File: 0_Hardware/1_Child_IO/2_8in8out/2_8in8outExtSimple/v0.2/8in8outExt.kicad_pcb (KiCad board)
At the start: 2 copper layers, 101.6 x 42 mm, 73 parts, among them P1 CONN_10X2, Q1 PNP, Q10 NPN, Q11 NPN, Q12 NPN, Q13 NPN, Q14 NPN, Q15 NPN, Q16 NPN, Q19 NPN, Q2 PNP, Q3 PNP, Q4 PNP, Q5 PNP, Q6 PNP, Q7 PNP, Q8 PNP, Q9 NPN, SW1 SKQGAKE010

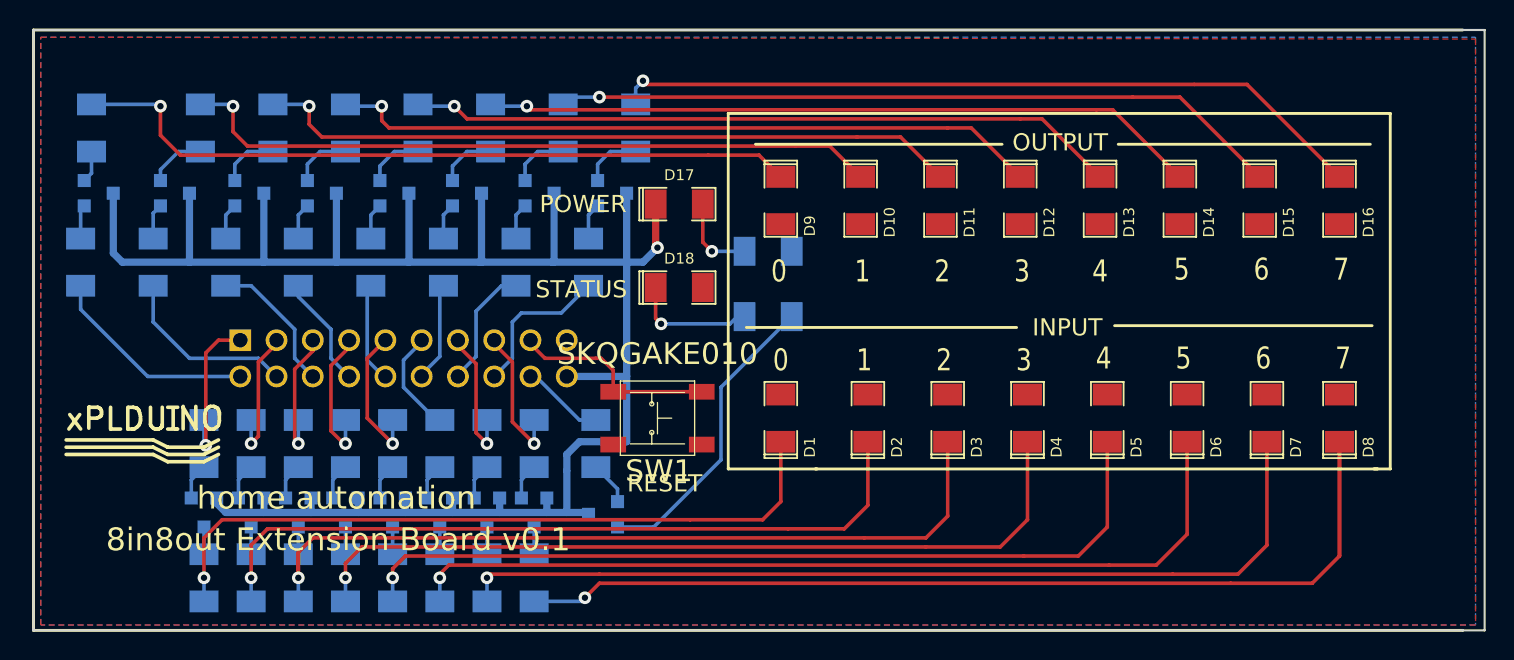
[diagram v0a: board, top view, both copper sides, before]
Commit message: IN8R8: remplacement empreinte PNP et NPN par SOT-23 standard, agencement des leds comme carte IN4DIM4
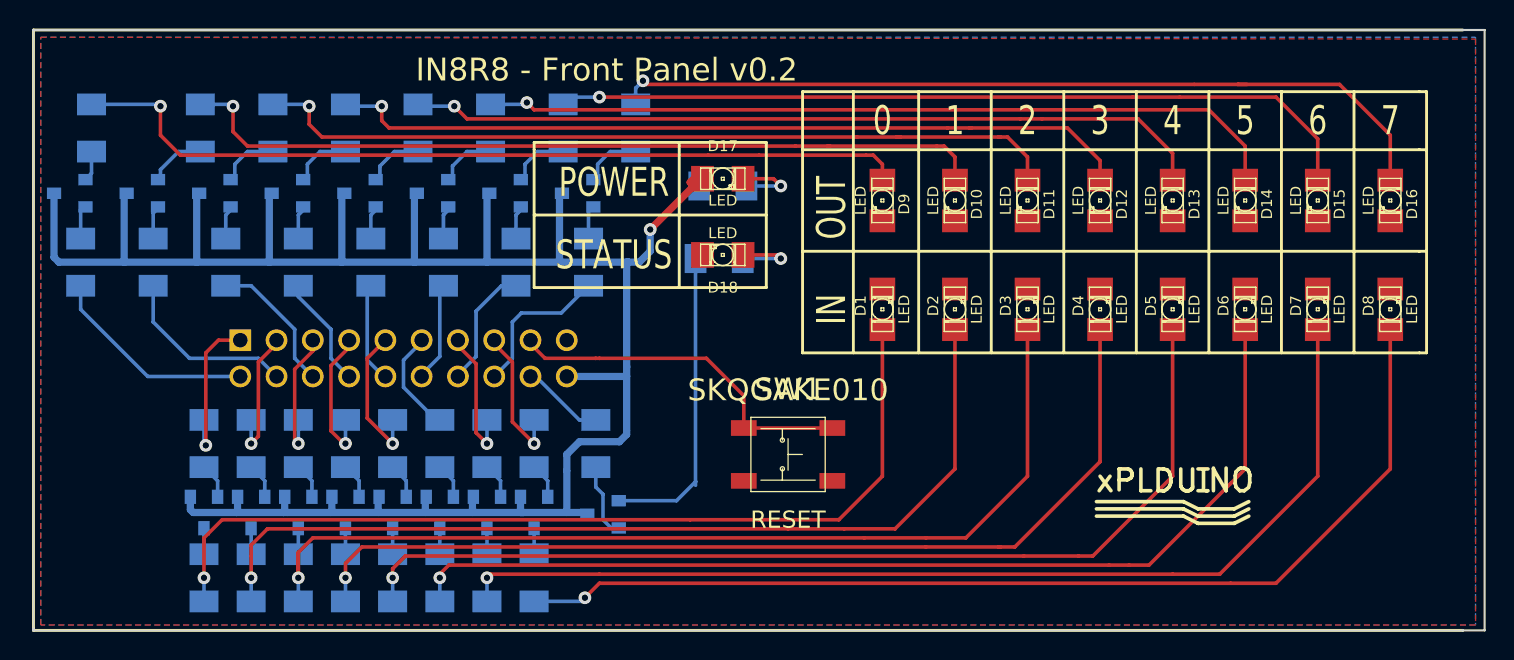
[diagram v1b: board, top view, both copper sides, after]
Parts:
- D1, D10, D11, D12, D13, D14, D15, D16, D17, D18, D2, D3, D4, D5, D6, D7, D8, D9: footprint SM1206POL -> LED-1206
- Q1, Q10, Q11, Q12, Q13, Q14, Q15, Q16, Q19, Q2, Q3, Q4, Q5, Q6, Q7, Q8, Q9: footprint SOT23EBC -> SOT23
- moved logo_xplduino 72.3 mm to (166.1, 107.2)
- moved D1 10.4 mm to (145.8, 93.5)
- moved D2 9.76 mm to (150.9, 93.5)
- moved SW1 9.49 mm to (139.2, 103.6)
- moved D3 9.45 mm to (156.0, 93.5)
- moved D4 9.16 mm to (161.0, 93.5)
- moved D5 8.89 mm to (166.1, 93.5)
- moved D6 8.64 mm to (171.2, 93.5)
- moved D7 8.41 mm to (176.3, 93.5)
- moved D8 8.41 mm to (181.4, 93.5)
- moved D9 7.11 mm to (145.8, 85.9)
- moved D10 6.60 mm to (150.9, 85.9)
- moved D11 6.10 mm to (156.0, 85.9)
- moved D12 5.59 mm to (161.0, 85.9)
- moved R41 5.57 mm to (134.6, 84.8), turned to 0 degrees
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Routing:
- net N-0000049: track 50.1 -> 64.2 mm
- net N-0000051: track 52.7 -> 65.2 mm
- net N-0000064: track 56.9 -> 68.7 mm
- net +5V: track 141.0 -> 152.2 mm
- net N-0000065: track 57.1 -> 67.8 mm
- net RESET: track 14.5 -> 25.2 mm
- net N-0000071: track 59.5 -> 69.8 mm
- net N-0000058: track 61.9 -> 71.1 mm
- net N-0000055: track 64.4 -> 73.0 mm
- net N-0000060: track 51.6 -> 59.4 mm
- net N-0000022: track 49.4 -> 57.2 mm
- net N-0000017: track 49.6 -> 57.1 mm
- net N-0000029: track 49.9 -> 56.6 mm
- net N-0000010: track 49.9 -> 56.1 mm
- net N-000006: track 50.4 -> 56.5 mm
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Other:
- board text added: "IN"
- board text added: "IN8R8 - Front Panel v0.2"
- board text added: "OUT"
- board text removed: "8in8out Extension Board v0.1"
- board text removed: "INPUT"
- board text removed: "OUTPUT"
- board text removed: "home automation"

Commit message: skilkscreen + gerber
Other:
- board text added: "."
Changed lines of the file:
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@@
     (area 76.964334 69.045001 188.035001 116.3345)
     (thickness 1.6)
-    (drawings 61)
-    (tracks 401)
+    (drawings 79)
+    (tracks 403)
     (zones 0)
     (modules 73)
@@
     (18 B.Paste user)
     (19 F.Paste user)
-    (20 B.SilkS user hide)
+    (20 B.SilkS user)
     (21 F.SilkS user)
     (22 B.Mask user)
@@
       (plotothertext true)
       (plotinvisibletext false)
-      (padsonsilk false)
+      (padsonsilk true)
       (subtractmaskfromsilk false)
       (outputformat 1)
@@
   (module SKQGAKE010 (layer F.Cu)
     (at 139.192 103.632 180)
-    (fp_text reference SW1 (at 0 4.572 180) (layer F.SilkS)
+    (fp_text reference SW1 (at 0 -0.254 180) (layer F.SilkS)
       (effects (font (size 1.524 1.524) (thickness 0.3048)))
     )
@@
     (tags "LED1206 SMD")
     (attr smd)
-    (fp_text reference D7 (at 0.254 -1.524 90) (layer F.SilkS)
+    (fp_text reference D7 (at -1.524 0.254 90) (layer F.SilkS)
       (effects (font (size 0.762 0.762) (thickness 0.0889)))
     )
@@
     (tags "LED1206 SMD")
     (attr smd)
-    (fp_text reference D2 (at 0.254 -1.524 90) (layer F.SilkS)
+    (fp_text reference D2 (at -1.651 0.127 90) (layer F.SilkS)
       (effects (font (size 0.762 0.762) (thickness 0.0889)))
     )
@@
     (tags "LED1206 SMD")
     (attr smd)
-    (fp_text reference D18 (at 0 -2.286 180) (layer F.SilkS)
+    (fp_text reference D18 (at 0.127 0.127 180) (layer F.SilkS)
       (effects (font (size 0.762 0.762) (thickness 0.0889)))
     )
@@
     (tags "LED1206 SMD")
     (attr smd)
-    (fp_text reference D3 (at 0.254 -1.524 90) (layer F.SilkS)
+    (fp_text reference D3 (at -1.651 0.127 90) (layer F.SilkS)
       (effects (font (size 0.762 0.762) (thickness 0.0889)))
     )
@@
     (tags "LED1206 SMD")
     (attr smd)
-    (fp_text reference D17 (at 0 -2.286) (layer F.SilkS)
+    (fp_text reference D17 (at -0.127 0.127) (layer F.SilkS)
       (effects (font (size 0.762 0.762) (thickness 0.0889)))
     )
@@
     (tags "LED1206 SMD")
     (attr smd)
-    (fp_text reference D4 (at 0.254 -1.524 90) (layer F.SilkS)
+    (fp_text reference D4 (at -1.524 0 90) (layer F.SilkS)
       (effects (font (size 0.762 0.762) (thickness 0.0889)))
     )
@@
     (tags "LED1206 SMD")
     (attr smd)
-    (fp_text reference D5 (at 0.254 -1.524 90) (layer F.SilkS)
+    (fp_text reference D5 (at -1.524 0 90) (layer F.SilkS)
       (effects (font (size 0.762 0.762) (thickness 0.0889)))
     )
@@
     (tags "LED1206 SMD")
     (attr smd)
-    (fp_text reference D6 (at 0.254 -1.524 90) (layer F.SilkS)
+    (fp_text reference D6 (at -1.651 0 90) (layer F.SilkS)
       (effects (font (size 0.762 0.762) (thickness 0.0889)))
     )
@@
     (tags "LED1206 SMD")
     (attr smd)
-    (fp_text reference D12 (at 0.254 -1.524 270) (layer F.SilkS)
+    (fp_text reference D12 (at 1.397 -0.127 270) (layer F.SilkS)
       (effects (font (size 0.762 0.762) (thickness 0.0889)))
     )
@@
     (tags "LED1206 SMD")
     (attr smd)
-    (fp_text reference D8 (at 0.254 -1.524 90) (layer F.SilkS)
+    (fp_text reference D8 (at -1.524 0.127 90) (layer F.SilkS)
       (effects (font (size 0.762 0.762) (thickness 0.0889)))
     )
@@
     (tags "LED1206 SMD")
     (attr smd)
-    (fp_text reference D9 (at 0.254 -1.524 270) (layer F.SilkS)
+    (fp_text reference D9 (at 1.397 -0.254 270) (layer F.SilkS)
       (effects (font (size 0.762 0.762) (thickness 0.0889)))
     )
@@
     (tags "LED1206 SMD")
     (attr smd)
-    (fp_text reference D10 (at 0.254 -1.524 270) (layer F.SilkS)
+    (fp_text reference D10 (at 1.397 -0.127 270) (layer F.SilkS)
       (effects (font (size 0.762 0.762) (thickness 0.0889)))
     )
@@
     (tags "LED1206 SMD")
     (attr smd)
-    (fp_text reference D11 (at 0.254 -1.524 270) (layer F.SilkS)
+    (fp_text reference D11 (at 1.397 -0.127 270) (layer F.SilkS)
       (effects (font (size 0.762 0.762) (thickness 0.0889)))
     )
@@
     (tags "LED1206 SMD")
     (attr smd)
-    (fp_text reference D16 (at 0.254 -1.524 270) (layer F.SilkS)
+    (fp_text reference D16 (at 1.397 -0.635 270) (layer F.SilkS)
       (effects (font (size 0.762 0.762) (thickness 0.0889)))
     )
@@
     (tags "LED1206 SMD")
     (attr smd)
-    (fp_text reference D15 (at 0.254 -1.524 270) (layer F.SilkS)
+    (fp_text reference D15 (at 1.27 -0.635 270) (layer F.SilkS)
       (effects (font (size 0.762 0.762) (thickness 0.0889)))
     )
@@
     (tags "LED1206 SMD")
     (attr smd)
-    (fp_text reference D14 (at 0.254 -1.524 270) (layer F.SilkS)
+    (fp_text reference D14 (at 1.27 -0.635 270) (layer F.SilkS)
       (effects (font (size 0.762 0.762) (thickness 0.0889)))
     )
@@
     (tags "LED1206 SMD")
     (attr smd)
-    (fp_text reference D13 (at 0.254 -1.524 270) (layer F.SilkS)
+    (fp_text reference D13 (at 1.397 0.508 270) (layer F.SilkS)
       (effects (font (size 0.762 0.762) (thickness 0.0889)))
     )
@@
     )
   )
+  (gr_line (start 111.252 92.964) (end 113.284 92.964) (angle 90) (layer B.SilkS) (width 0.2))
+  (gr_text . (at 146.939 89.789) (layer F.SilkS)
+    (effects (font (size 2 2) (thickness 0.25)))
+  )
+  (gr_text . (at 146.939 88.011) (layer F.SilkS)
+    (effects (font (size 2 2) (thickness 0.25)))
+  )
+  (gr_text . (at 152.019 88.011) (layer F.SilkS)
+    (effects (font (size 2 2) (thickness 0.25)))
+  )
+  (gr_text . (at 152.019 89.789) (layer F.SilkS)
+    (effects (font (size 2 2) (thickness 0.25)))
+  )
+  (gr_text . (at 157.099 89.789) (layer F.SilkS)
+    (effects (font (size 2 2) (thickness 0.25)))
+  )
+  (gr_text . (at 157.099 88.011) (layer F.SilkS)
+    (effects (font (size 2 2) (thickness 0.25)))
+  )
+  (gr_text . (at 162.179 88.011) (layer F.SilkS)
+    (effects (font (size 2 2) (thickness 0.25)))
+  )
+  (gr_text . (at 162.179 89.789) (layer F.SilkS)
+    (effects (font (size 2 2) (thickness 0.25)))
+  )
+  (gr_text . (at 167.259 89.789) (layer F.SilkS)
+    (effects (font (size 2 2) (thickness 0.25)))
+  )
+  (gr_text . (at 172.339 89.789) (layer F.SilkS)
+    (effects (font (size 2 2) (thickness 0.25)))
+  )
+  (gr_text . (at 177.419 89.789) (layer F.SilkS)
+    (effects (font (size 2 2) (thickness 0.25)))
+  )
+  (gr_text . (at 167.259 88.011) (layer F.SilkS)
+    (effects (font (size 2 2) (thickness 0.25)))
+  )
+  (gr_text . (at 172.339 88.011) (layer F.SilkS)
+    (effects (font (size 2 2) (thickness 0.25)))
+  )
+  (gr_text . (at 177.419 88.011) (layer F.SilkS)
+    (effects (font (size 2 2) (thickness 0.25)))
+  )
+  (gr_text . (at 132.334 87.249) (layer F.SilkS)
+    (effects (font (size 2 2) (thickness 0.25)))
+  )
+  (gr_text . (at 137.033 85.471) (layer F.SilkS)
+    (effects (font (size 2 2) (thickness 0.25)))
+  )
+  (gr_text . (at 182.753 88.011) (layer F.SilkS)
+    (effects (font (size 2 2) (thickness 0.25)))
+  )
+  (gr_text . (at 182.753 89.789) (layer F.SilkS)
+    (effects (font (size 2 2) (thickness 0.25)))
+  )
   (gr_line (start 183.388 82.296) (end 183.896 82.296) (angle 90) (layer F.SilkS) (width 0.2))
   (gr_line (start 183.388 89.408) (end 183.896 89.408) (angle 90) (layer F.SilkS) (width 0.2))
@@
   )
   (gr_line (start 181.356 93.472) (end 181.356 83.82) (angle 90) (layer Cmts.User) (width 0.2))
-  (gr_line (start 111.252 92.964) (end 113.284 92.964) (angle 90) (layer F.Mask) (width 0.2))
   (gr_line (start 187.96 73.914) (end 187.96 115.951) (angle 90) (layer Edge.Cuts) (width 0.15))
   (gr_line (start 186.436 73.914) (end 187.96 73.914) (angle 90) (layer Edge.Cuts) (width 0.15))
@@
   (segment (start 110.617 83.439) (end 111.633 82.423) (width 0.254) (layer B.Cu) (net 63))
   (segment (start 111.633 82.423) (end 113.284 82.423) (width 0.254) (layer B.Cu) (net 63))
-  (segment (start 94.361 98.171) (end 100.838 98.171) (width 0.254) (layer B.Cu) (net 64))
-  (segment (start 89.662 91.821) (end 89.662 93.472) (width 0.254) (layer B.Cu) (net 64))
-  (segment (start 89.662 93.472) (end 94.361 98.171) (width 0.254) (layer B.Cu) (net 64))
+  (segment (start 89.662 91.821) (end 92.329 91.821) (width 0.254) (layer B.Cu) (net 64))
+  (segment (start 92.71 93.472) (end 97.409 98.171) (width 0.254) (layer B.Cu) (net 64))
+  (segment (start 92.71 92.202) (end 92.71 93.472) (width 0.254) (layer B.Cu) (net 64))
+  (segment (start 92.329 91.821) (end 92.71 92.202) (width 0.254) (layer B.Cu) (net 64))
+  (segment (start 97.409 98.171) (end 100.838 98.171) (width 0.254) (layer B.Cu) (net 64))
   (segment (start 102.108 96.901) (end 103.378 98.171) (width 0.254) (layer B.Cu) (net 65))
   (segment (start 97.282 96.901) (end 102.108 96.901) (width 0.254) (layer B.Cu) (net 65))
